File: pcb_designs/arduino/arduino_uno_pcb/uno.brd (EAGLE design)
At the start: 73.3 x 63.5 mm, 25 parts, among them IC1 ATMEGA328, IC2 7805, Q1 12MHZ

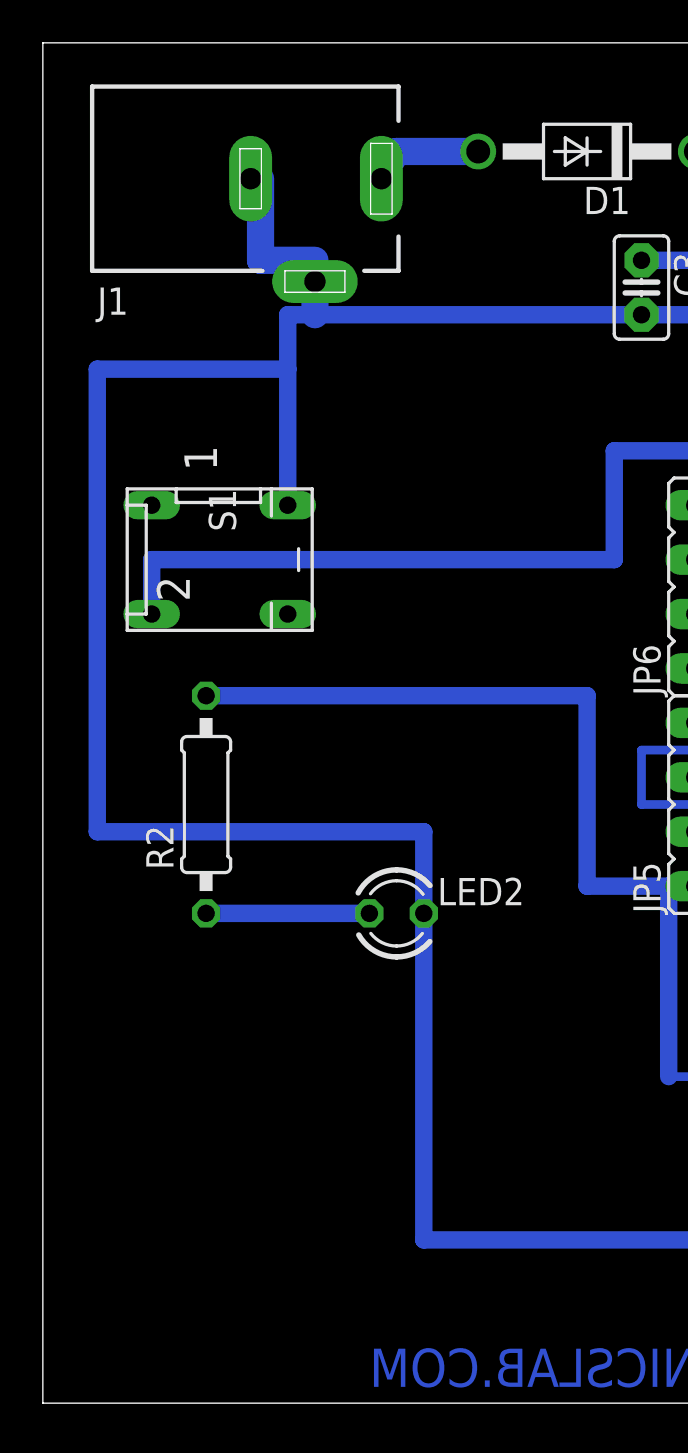
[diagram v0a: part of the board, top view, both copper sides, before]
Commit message: ADD arduino_uno_pcb _with_lcd
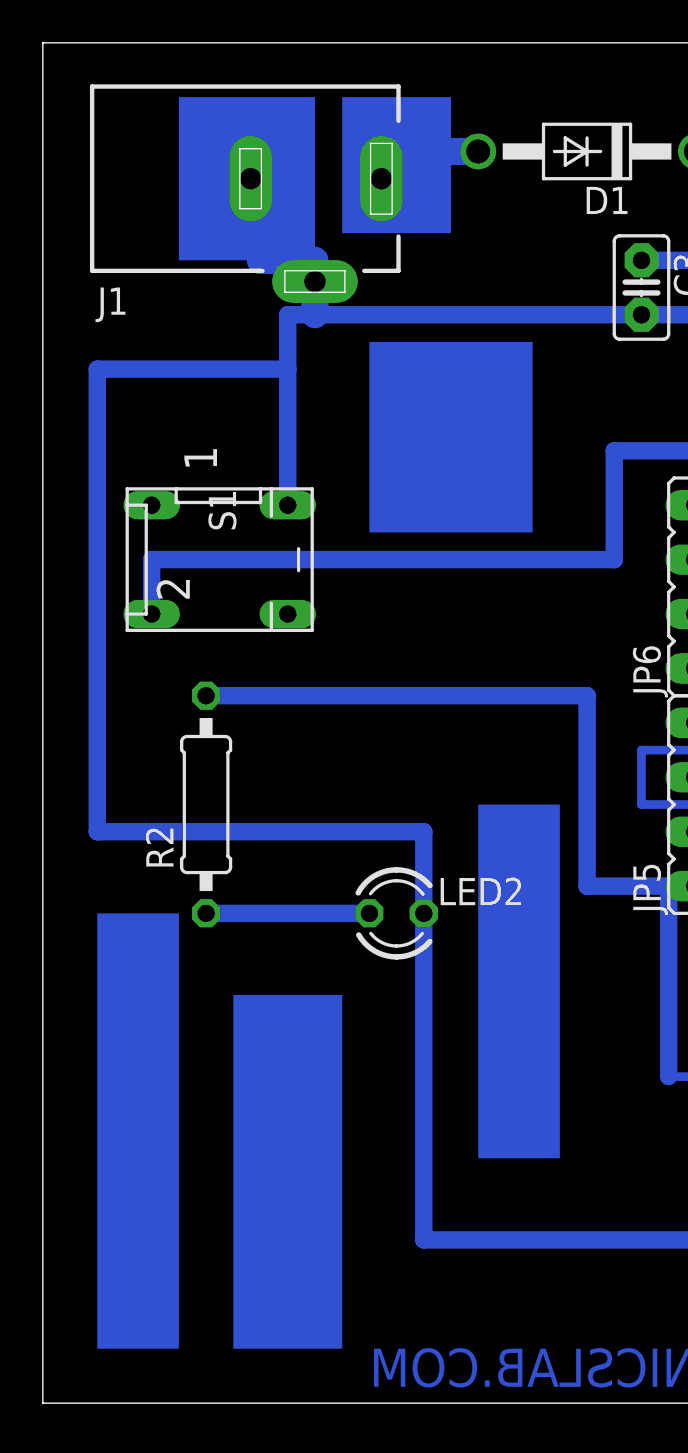
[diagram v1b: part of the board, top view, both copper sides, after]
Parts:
- Q1: value 12MHZ -> 16MHZ
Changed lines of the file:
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@@
 <grid distance="0.05" unitdist="inch" unit="inch" style="lines" multiple="1" display="no" altdistance="0.025" altunitdist="inch" altunit="inch"/>
 <layers>
-<layer number="1" name="Top" color="4" fill="1" visible="no" active="yes"/>
-<layer number="16" name="Bottom" color="1" fill="1" visible="yes" active="yes"/>
+<layer number="1" name="Top" color="4" fill="1" visible="yes" active="yes"/>
+<layer number="16" name="Bottom" color="1" fill="1" visible="no" active="yes"/>
 <layer number="17" name="Pads" color="2" fill="1" visible="yes" active="yes"/>
 <layer number="18" name="Vias" color="2" fill="1" visible="yes" active="yes"/>
 <layer number="19" name="Unrouted" color="6" fill="1" visible="yes" active="yes"/>
 <layer number="20" name="Dimension" color="15" fill="1" visible="yes" active="yes"/>
-<layer number="21" name="tPlace" color="7" fill="1" visible="no" active="yes"/>
-<layer number="22" name="bPlace" color="7" fill="1" visible="no" active="yes"/>
+<layer number="21" name="tPlace" color="7" fill="1" visible="yes" active="yes"/>
+<layer number="22" name="bPlace" color="7" fill="1" visible="yes" active="yes"/>
 <layer number="23" name="tOrigins" color="15" fill="1" visible="no" active="yes"/>
-<layer number="24" name="bOrigins" color="15" fill="1" visible="no" active="yes"/>
-<layer number="25" name="tNames" color="7" fill="1" visible="no" active="yes"/>
-<layer number="26" name="bNames" color="7" fill="1" visible="no" active="yes"/>
-<layer number="27" name="tValues" color="7" fill="1" visible="no" active="yes"/>
-<layer number="28" name="bValues" color="7" fill="1" visible="no" active="yes"/>
-<layer number="29" name="tStop" color="7" fill="3" visible="no" active="yes"/>
-<layer number="30" name="bStop" color="7" fill="6" visible="no" active="yes"/>
-<layer number="31" name="tCream" color="7" fill="4" visible="no" active="yes"/>
-<layer number="32" name="bCream" color="7" fill="5" visible="no" active="yes"/>
-<layer number="33" name="tFinish" color="6" fill="3" visible="no" active="yes"/>
-<layer number="34" name="bFinish" color="6" fill="6" visible="no" active="yes"/>
-<layer number="35" name="tGlue" color="7" fill="4" visible="no" active="yes"/>
-<layer number="36" name="bGlue" color="7" fill="5" visible="no" active="yes"/>
-<layer number="37" name="tTest" color="7" fill="1" visible="no" active="yes"/>
-<layer number="38" name="bTest" color="7" fill="1" visible="no" active="yes"/>
-<layer number="39" name="tKeepout" color="4" fill="11" visible="no" active="yes"/>
-<layer number="40" name="bKeepout" color="1" fill="11" visible="no" active="yes"/>
-<layer number="41" name="tRestrict" color="4" fill="10" visible="no" active="yes"/>
-<layer number="42" name="bRestrict" color="1" fill="10" visible="no" active="yes"/>
-<layer number="43" name="vRestrict" color="2" fill="10" visible="no" active="yes"/>
-<layer number="44" name="Drills" color="7" fill="1" visible="no" active="yes"/>
-<layer number="45" name="Holes" color="7" fill="1" visible="no" active="yes"/>
-<layer number="46" name="Milling" color="3" fill="1" visible="no" active="yes"/>
-<layer number="47" name="Measures" color="7" fill="1" visible="no" active="yes"/>
-<layer number="48" name="Document" color="7" fill="1" visible="no" active="yes"/>
-<layer number="49" name="Reference" color="7" fill="1" visible="no" active="yes"/>
-<layer number="51" name="tDocu" color="7" fill="1" visible="no" active="yes"/>
-<layer number="52" name="bDocu" color="7" fill="1" visible="no" active="yes"/>
+<layer number="24" name="bOrigins" color="15" fill="1" visible="yes" active="yes"/>
+<layer number="25" name="tNames" color="7" fill="1" visible="yes" active="yes"/>
+<layer number="26" name="bNames" color="7" fill="1" visible="yes" active="yes"/>
+<layer number="27" name="tValues" color="7" fill="1" visible="yes" active="yes"/>
+<layer number="28" name="bValues" color="7" fill="1" visible="yes" active="yes"/>
+<layer number="29" name="tStop" color="7" fill="3" visible="yes" active="yes"/>
+<layer number="30" name="bStop" color="7" fill="6" visible="yes" active="yes"/>
+<layer number="31" name="tCream" color="7" fill="4" visible="yes" active="yes"/>
+<layer number="32" name="bCream" color="7" fill="5" visible="yes" active="yes"/>
+<layer number="33" name="tFinish" color="6" fill="3" visible="yes" active="yes"/>
+<layer number="34" name="bFinish" color="6" fill="6" visible="yes" active="yes"/>
+<layer number="35" name="tGlue" color="7" fill="4" visible="yes" active="yes"/>
+<layer number="36" name="bGlue" color="7" fill="5" visible="yes" active="yes"/>
+<layer number="37" name="tTest" color="7" fill="1" visible="yes" active="yes"/>
+<layer number="38" name="bTest" color="7" fill="1" visible="yes" active="yes"/>
+<layer number="39" name="tKeepout" color="4" fill="11" visible="yes" active="yes"/>
+<layer number="40" name="bKeepout" color="1" fill="11" visible="yes" active="yes"/>
+<layer number="41" name="tRestrict" color="4" fill="10" visible="yes" active="yes"/>
+<layer number="42" name="bRestrict" color="1" fill="10" visible="yes" active="yes"/>
+<layer number="43" name="vRestrict" color="2" fill="10" visible="yes" active="yes"/>
+<layer number="44" name="Drills" color="7" fill="1" visible="yes" active="yes"/>
+<layer number="45" name="Holes" color="7" fill="1" visible="yes" active="yes"/>
+<layer number="46" name="Milling" color="3" fill="1" visible="yes" active="yes"/>
+<layer number="47" name="Measures" color="7" fill="1" visible="yes" active="yes"/>
+<layer number="48" name="Document" color="7" fill="1" visible="yes" active="yes"/>
+<layer number="49" name="Reference" color="7" fill="1" visible="yes" active="yes"/>
+<layer number="51" name="tDocu" color="7" fill="1" visible="yes" active="yes"/>
+<layer number="52" name="bDocu" color="7" fill="1" visible="yes" active="yes"/>
 <layer number="53" name="tGND_GNDA" color="7" fill="9" visible="no" active="no"/>
 <layer number="54" name="bGND_GNDA" color="1" fill="9" visible="no" active="no"/>
@@
 <wire x1="5.08" y1="80" x2="5.08" y2="16.51" width="0" layer="20"/>
 <text x="20.32" y="19.05" size="1.778" layer="16" rot="MR180">WWW.COMPUTRONICSLAB.COM</text>
+<rectangle x1="11.43" y1="69.85" x2="17.78" y2="77.47" layer="16"/>
+<rectangle x1="19.05" y1="71.12" x2="24.13" y2="77.47" layer="16"/>
+<rectangle x1="20.32" y1="57.15" x2="27.94" y2="66.04" layer="16"/>
+<rectangle x1="25.4" y1="27.94" x2="29.21" y2="44.45" layer="16"/>
+<rectangle x1="7.62" y1="19.05" x2="11.43" y2="39.37" layer="16"/>
+<rectangle x1="13.97" y1="19.05" x2="19.05" y2="35.56" layer="16"/>
 </plain>
 <attributes>
@@
 <attribute name="OC_FARNELL" value="unknown" x="6.35" y="53.34" size="1.778" layer="27" rot="R270" display="off"/>
 </element>
-<element name="Q1" library="crystal" package="HC49/S" value="12MHZ" x="41.91" y="33.02" rot="R90">
+<element name="Q1" library="crystal" package="HC49/S" value="16MHZ" x="41.91" y="33.02" rot="R90">
 <attribute name="OC_NEWARK" value="unknown" x="74.93" y="72.39" size="1.778" layer="27" rot="R90" display="off"/>
 <attribute name="MPN" value="" x="74.93" y="72.39" size="1.778" layer="27" rot="R90" display="off"/>

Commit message: modify
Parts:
- added JP9: (no value), jumper:JP2
- moved D1 1.27 mm to (30.5, 73.7)
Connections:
- net N$7: now also JP9.1, JP9.2, JP9.3
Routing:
- net N$7: track 24.1 -> 38.1 mm
- net N$3: track 5.26 -> 6.53 mm
